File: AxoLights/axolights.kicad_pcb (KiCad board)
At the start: 2 copper layers, 100 x 50 mm, 54 parts, among them IC1 ATTINY85-S, P1 CONN_01X07, Q1 BSS138, Q2 BSS138, Q3 BSS138, Q4 BSS138, Q5 BSS138, Q6 BSS138, Q7 BSS138, Q8 BSS138

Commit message: started routing
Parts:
- removed IC1: ATTINY85-S, Housings_SOIC:SOIJ-8_5.3x5.3mm_Pitch1.27mm
- added P2: CONN_01X07, Connectors_JST:JST_EH_S07B-EH_07x2.50mm_Angled, B.Cu at (202.5, 71.5)
- P1: footprint Pin_Headers:Pin_Header_Straight_1x07_Pitch2.54mm -> Connectors_JST:JST_EH_S07B-EH_07x2.50mm_Angled; moved to B.Cu
- moved P1 89.0 mm to (116.5, 56.5), turned to 270 degrees
- moved Q7 18.0 mm to (202.2, 49.8)
- moved R13 18.0 mm to (205.8, 49.8)
- moved Q8 18.0 mm to (202.0, 78.2)
- moved R15 18.0 mm to (205.0, 78.2)
- moved Q6 14.3 mm to (190.8, 84.5)
- moved R10 14.3 mm to (190.8, 87.5)
- moved Q5 11.9 mm to (178.2, 84.5)
- moved R5 11.9 mm to (178.2, 87.5)
- moved D16 10.2 mm to (190.8, 51.5)
- moved D17 10.2 mm to (190.8, 64.0)
- moved D18 10.2 mm to (190.8, 76.5)
- moved R12 10.2 mm to (190.8, 43.5)
- moved R14 9.92 mm to (116.5, 50.0)
- moved R16 9.92 mm to (116.5, 78.0)
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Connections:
- Q1 pad 1: /AxoLights LEDs/WW -> WW
- Q2 pad 1: /AxoLights LEDs/WW -> WW
- Q3 pad 1: /AxoLights LEDs/NW -> NW
- Q4 pad 1: /AxoLights LEDs/NW -> NW
- Q5 pad 1: /AxoLights LEDs/NW -> NW
- Q6 pad 1: /AxoLights LEDs/KW -> KW
- Q7 pad 1: /AxoLights LEDs/Rt -> Rt
- Q8 pad 1: /AxoLights LEDs/Bl -> Bl
- R1 pad 2: /AxoLights LEDs/WW -> WW
- R10 pad 2: /AxoLights LEDs/KW -> KW
- R13 pad 2: /AxoLights LEDs/Rt -> Rt
- R15 pad 2: /AxoLights LEDs/Bl -> Bl
- R2 pad 2: /AxoLights LEDs/WW -> WW
- R5 pad 2: /AxoLights LEDs/NW -> NW
- R6 pad 2: /AxoLights LEDs/NW -> NW
- R9 pad 2: /AxoLights LEDs/NW -> NW
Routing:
- net GND: track 0.00 -> 151.4 mm, vias 0 -> 7
- net +12V: track 0.00 -> 151.1 mm, vias 0 -> 1
- net Bl: track 0.00 -> 25.4 mm
- net Net-(D23-Pad2): track 0.00 -> 22.5 mm, vias 0 -> 2
- net Net-(D22-Pad2): track 0.00 -> 22.5 mm, vias 0 -> 2
- net Net-(D20-Pad1): track 0.00 -> 22.5 mm, vias 0 -> 2
- net Net-(D19-Pad1): track 0.00 -> 22.5 mm, vias 0 -> 2
- net Net-(D24-Pad2): track 0.00 -> 21.6 mm, vias 0 -> 2
- net Net-(D19-Pad2): track 0.00 -> 18.8 mm, vias 0 -> 2
- net Net-(D21-Pad1): track 0.00 -> 18.6 mm, vias 0 -> 2
- net Net-(D22-Pad1): track 0.00 -> 18.3 mm, vias 0 -> 2
- net Rt: track 0.00 -> 14.5 mm, vias 0 -> 1
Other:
- outline, holes or cut-outs redrawn
- net class Default: trace_width 0.25 -> 0.4
- net class Power: trace_width 1 -> 0.75

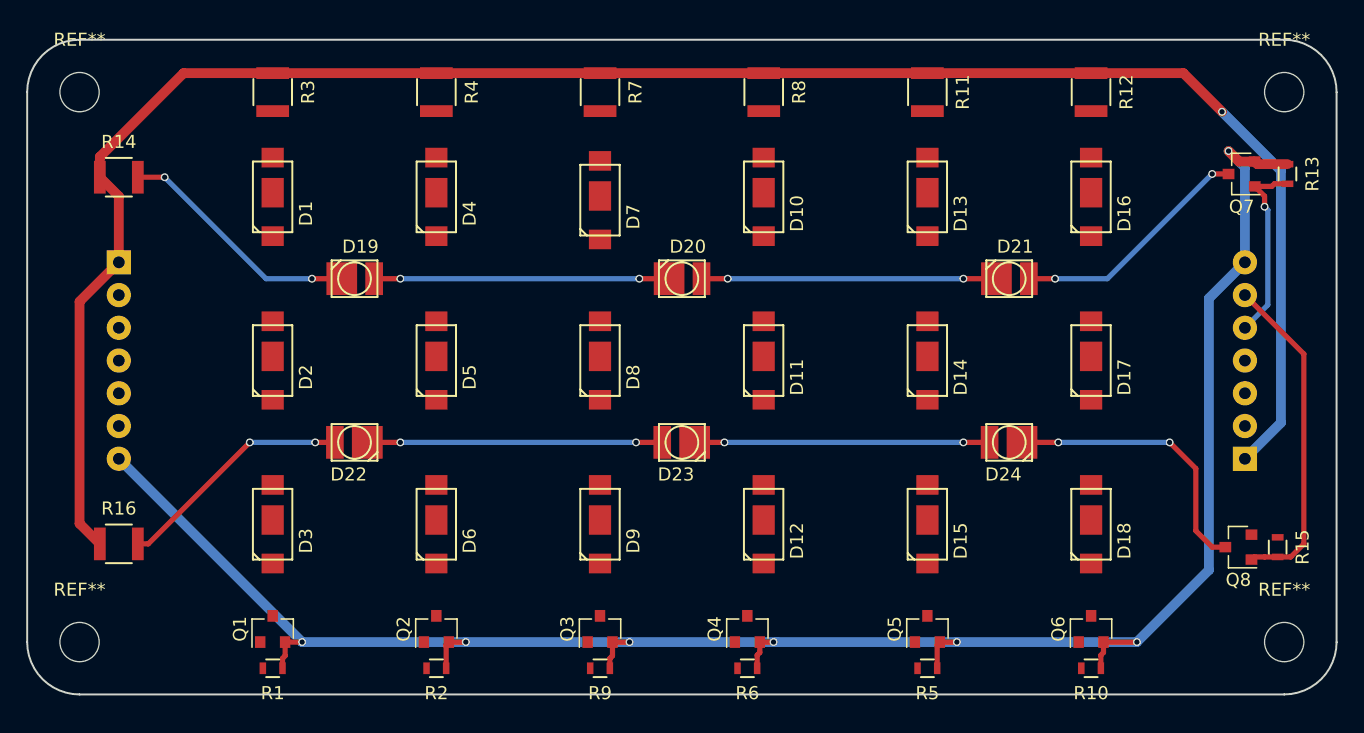
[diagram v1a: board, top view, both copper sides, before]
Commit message: Heatsinks started
started to layout heatsinking planes for LEDs
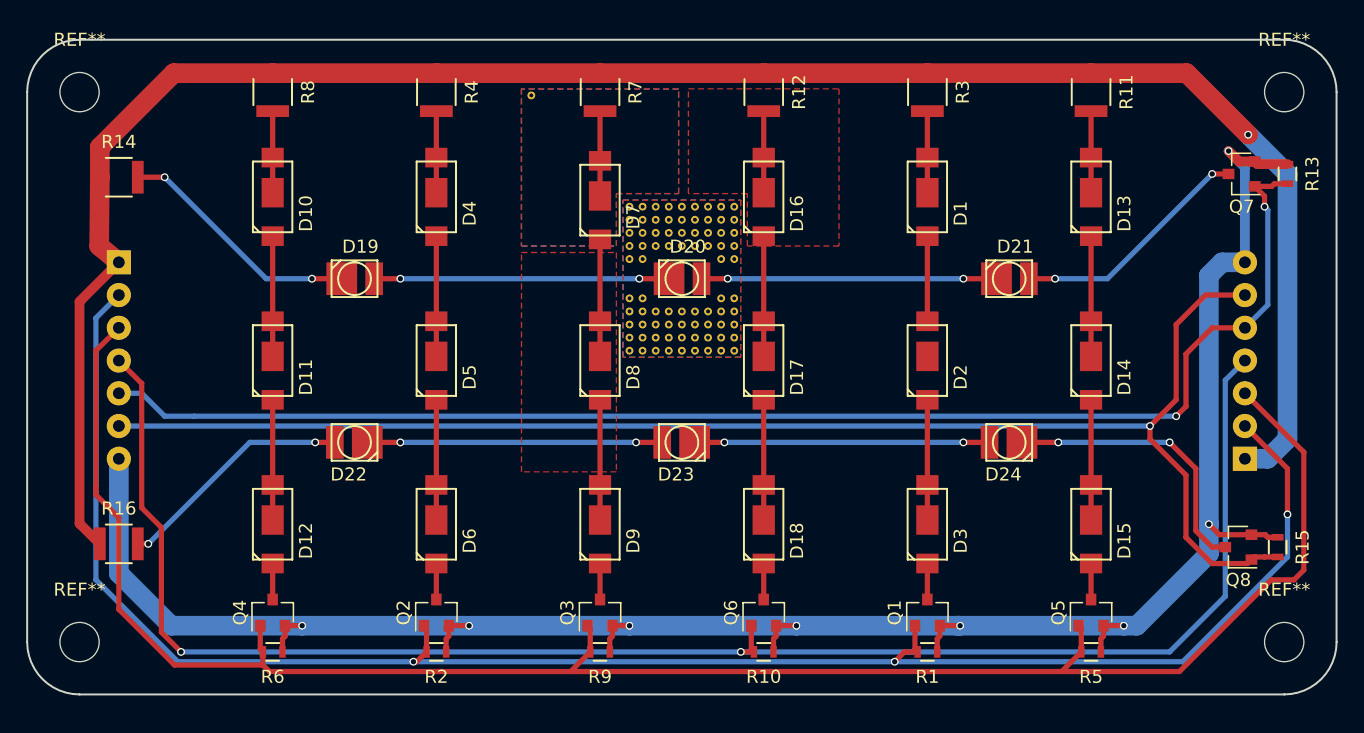
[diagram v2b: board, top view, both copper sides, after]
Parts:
- added REF**: ThermalVia, myfootprint:ThermalVia-0.6, F.Cu at (148.0, 43.8)
- added REF**: ThermalVia, myfootprint:ThermalVia-0.6, F.Cu at (157.5, 63.2)
- added REF**: ThermalVia, myfootprint:ThermalVia-0.6, F.Cu at (156.5, 63.2)
- added REF**: ThermalVia, myfootprint:ThermalVia-0.6, F.Cu at (155.5, 63.2)
- added REF**: ThermalVia, myfootprint:ThermalVia-0.6, F.Cu at (163.5, 62.2)
- added REF**: ThermalVia, myfootprint:ThermalVia-0.6, F.Cu at (162.5, 62.2)
- added REF**: ThermalVia, myfootprint:ThermalVia-0.6, F.Cu at (161.5, 62.2)
- added REF**: ThermalVia, myfootprint:ThermalVia-0.6, F.Cu at (160.5, 62.2)
- added REF**: ThermalVia, myfootprint:ThermalVia-0.6, F.Cu at (159.5, 62.2)
- added REF**: ThermalVia, myfootprint:ThermalVia-0.6, F.Cu at (158.5, 62.2)
- added REF**: ThermalVia, myfootprint:ThermalVia-0.6, F.Cu at (157.5, 62.2)
- added REF**: ThermalVia, myfootprint:ThermalVia-0.6, F.Cu at (158.5, 57.2)
- added REF**: ThermalVia, myfootprint:ThermalVia-0.6, F.Cu at (156.5, 62.2)
- added REF**: ThermalVia, myfootprint:ThermalVia-0.6, F.Cu at (155.5, 62.2)
- added REF**: ThermalVia, myfootprint:ThermalVia-0.6, F.Cu at (163.5, 61.2)
- added REF**: ThermalVia, myfootprint:ThermalVia-0.6, F.Cu at (162.5, 61.2)
- added REF**: ThermalVia, myfootprint:ThermalVia-0.6, F.Cu at (161.5, 61.2)
- added REF**: ThermalVia, myfootprint:ThermalVia-0.6, F.Cu at (160.5, 61.2)
- added REF**: ThermalVia, myfootprint:ThermalVia-0.6, F.Cu at (159.5, 61.2)
- added REF**: ThermalVia, myfootprint:ThermalVia-0.6, F.Cu at (158.5, 61.2)
- added REF**: ThermalVia, myfootprint:ThermalVia-0.6, F.Cu at (157.5, 61.2)
- added REF**: ThermalVia, myfootprint:ThermalVia-0.6, F.Cu at (156.5, 61.2)
- added REF**: ThermalVia, myfootprint:ThermalVia-0.6, F.Cu at (158.5, 58.2)
- added REF**: ThermalVia, myfootprint:ThermalVia-0.6, F.Cu at (155.5, 61.2)
- added REF**: ThermalVia, myfootprint:ThermalVia-0.6, F.Cu at (163.5, 60.2)
- added REF**: ThermalVia, myfootprint:ThermalVia-0.6, F.Cu at (162.5, 60.2)
- added REF**: ThermalVia, myfootprint:ThermalVia-0.6, F.Cu at (161.5, 60.2)
- added REF**: ThermalVia, myfootprint:ThermalVia-0.6, F.Cu at (160.5, 60.2)
- added REF**: ThermalVia, myfootprint:ThermalVia-0.6, F.Cu at (159.5, 60.2)
- added REF**: ThermalVia, myfootprint:ThermalVia-0.6, F.Cu at (158.5, 60.2)
- added REF**: ThermalVia, myfootprint:ThermalVia-0.6, F.Cu at (157.5, 60.2)
- added REF**: ThermalVia, myfootprint:ThermalVia-0.6, F.Cu at (156.5, 60.2)
- added REF**: ThermalVia, myfootprint:ThermalVia-0.6, F.Cu at (155.5, 60.2)
- added REF**: ThermalVia, myfootprint:ThermalVia-0.6, F.Cu at (163.5, 63.2)
- added REF**: ThermalVia, myfootprint:ThermalVia-0.6, F.Cu at (163.5, 59.2)
- added REF**: ThermalVia, myfootprint:ThermalVia-0.6, F.Cu at (162.5, 59.2)
- added REF**: ThermalVia, myfootprint:ThermalVia-0.6, F.Cu at (156.5, 59.2)
- added REF**: ThermalVia, myfootprint:ThermalVia-0.6, F.Cu at (155.5, 59.2)
- added REF**: ThermalVia, myfootprint:ThermalVia-0.6, F.Cu at (163.5, 56.2)
- added REF**: ThermalVia, myfootprint:ThermalVia-0.6, F.Cu at (162.5, 56.2)
- added REF**: ThermalVia, myfootprint:ThermalVia-0.6, F.Cu at (157.5, 56.2)
- added REF**: ThermalVia, myfootprint:ThermalVia-0.6, F.Cu at (156.5, 56.2)
- added REF**: ThermalVia, myfootprint:ThermalVia-0.6, F.Cu at (155.5, 56.2)
- added REF**: ThermalVia, myfootprint:ThermalVia-0.6, F.Cu at (163.5, 55.2)
- added REF**: ThermalVia, myfootprint:ThermalVia-0.6, F.Cu at (162.5, 63.2)
- added REF**: ThermalVia, myfootprint:ThermalVia-0.6, F.Cu at (162.5, 55.2)
- added REF**: ThermalVia, myfootprint:ThermalVia-0.6, F.Cu at (161.5, 55.2)
- added REF**: ThermalVia, myfootprint:ThermalVia-0.6, F.Cu at (160.5, 55.2)
- added REF**: ThermalVia, myfootprint:ThermalVia-0.6, F.Cu at (159.5, 55.2)
- added REF**: ThermalVia, myfootprint:ThermalVia-0.6, F.Cu at (158.5, 55.2)
- added REF**: ThermalVia, myfootprint:ThermalVia-0.6, F.Cu at (157.5, 55.2)
- added REF**: ThermalVia, myfootprint:ThermalVia-0.6, F.Cu at (156.5, 55.2)
- added REF**: ThermalVia, myfootprint:ThermalVia-0.6, F.Cu at (155.5, 55.2)
- added REF**: ThermalVia, myfootprint:ThermalVia-0.6, F.Cu at (163.5, 54.2)
- added REF**: ThermalVia, myfootprint:ThermalVia-0.6, F.Cu at (162.5, 54.2)
- added REF**: ThermalVia, myfootprint:ThermalVia-0.6, F.Cu at (161.5, 63.2)
- added REF**: ThermalVia, myfootprint:ThermalVia-0.6, F.Cu at (161.5, 54.2)
- added REF**: ThermalVia, myfootprint:ThermalVia-0.6, F.Cu at (160.5, 54.2)
- added REF**: ThermalVia, myfootprint:ThermalVia-0.6, F.Cu at (159.5, 54.2)
- added REF**: ThermalVia, myfootprint:ThermalVia-0.6, F.Cu at (158.5, 54.2)
- added REF**: ThermalVia, myfootprint:ThermalVia-0.6, F.Cu at (157.5, 54.2)
- added REF**: ThermalVia, myfootprint:ThermalVia-0.6, F.Cu at (156.5, 54.2)
- added REF**: ThermalVia, myfootprint:ThermalVia-0.6, F.Cu at (155.5, 54.2)
- added REF**: ThermalVia, myfootprint:ThermalVia-0.6, F.Cu at (163.5, 53.2)
- added REF**: ThermalVia, myfootprint:ThermalVia-0.6, F.Cu at (162.5, 53.2)
- added REF**: ThermalVia, myfootprint:ThermalVia-0.6, F.Cu at (161.5, 53.2)
- added REF**: ThermalVia, myfootprint:ThermalVia-0.6, F.Cu at (160.5, 63.2)
- added REF**: ThermalVia, myfootprint:ThermalVia-0.6, F.Cu at (160.5, 53.2)
- added REF**: ThermalVia, myfootprint:ThermalVia-0.6, F.Cu at (159.5, 53.2)
- added REF**: ThermalVia, myfootprint:ThermalVia-0.6, F.Cu at (158.5, 53.2)
- added REF**: ThermalVia, myfootprint:ThermalVia-0.6, F.Cu at (157.5, 53.2)
- added REF**: ThermalVia, myfootprint:ThermalVia-0.6, F.Cu at (156.5, 53.2)
- added REF**: ThermalVia, myfootprint:ThermalVia-0.6, F.Cu at (155.5, 53.2)
- added REF**: ThermalVia, myfootprint:ThermalVia-0.6, F.Cu at (163.5, 52.2)
- added REF**: ThermalVia, myfootprint:ThermalVia-0.6, F.Cu at (162.5, 52.2)
- added REF**: ThermalVia, myfootprint:ThermalVia-0.6, F.Cu at (161.5, 52.2)
- added REF**: ThermalVia, myfootprint:ThermalVia-0.6, F.Cu at (160.5, 52.2)
- added REF**: ThermalVia, myfootprint:ThermalVia-0.6, F.Cu at (159.5, 63.2)
- added REF**: ThermalVia, myfootprint:ThermalVia-0.6, F.Cu at (159.5, 52.2)
- added REF**: ThermalVia, myfootprint:ThermalVia-0.6, F.Cu at (158.5, 52.2)
- added REF**: ThermalVia, myfootprint:ThermalVia-0.6, F.Cu at (157.5, 52.2)
- added REF**: ThermalVia, myfootprint:ThermalVia-0.6, F.Cu at (156.5, 52.2)
- added REF**: ThermalVia, myfootprint:ThermalVia-0.6, F.Cu at (155.5, 52.2)
- added REF**: ThermalVia, myfootprint:ThermalVia-0.6, F.Cu at (158.5, 63.2)
- moved Q1 50.0 mm to (178.2, 83.2)
- moved R1 50.0 mm to (178.2, 86.2)
- moved D1 50.0 mm to (178.2, 51.5)
- moved D2 50.0 mm to (178.2, 64.0)
- moved D3 50.0 mm to (178.2, 76.5)
- moved R3 50.0 mm to (178.2, 43.5)
- moved D10 37.5 mm to (128.2, 51.5)
- moved D11 37.5 mm to (128.2, 64.0)
- moved D12 37.5 mm to (128.2, 76.5)
- moved R8 37.5 mm to (128.2, 43.5)
- moved Q4 36.3 mm to (128.2, 83.2)
- moved R6 36.3 mm to (128.2, 86.2)
- moved Q6 25.0 mm to (165.8, 83.2)
- moved R10 25.0 mm to (165.8, 86.2)
- moved D16 25.0 mm to (165.8, 51.5)
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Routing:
- net NW: track 0.00 -> 145.8 mm
- net WW: track 0.00 -> 138.3 mm, vias 0 -> 3
- net KW: track 0.00 -> 127.4 mm, vias 0 -> 2
- net Rt: track 14.5 -> 106.4 mm, vias 1 -> 2
- net Bl: track 25.4 -> 111.2 mm, vias 0 -> 1
- net GND: track 151.4 -> 162.0 mm, vias 7 -> 8
- net Net-(D8-Pad2): track 0.00 -> 9.18 mm
- net Net-(D5-Pad2): track 0.00 -> 9.18 mm
- net Net-(D2-Pad2): track 0.00 -> 9.18 mm
- net Net-(D17-Pad2): track 0.00 -> 9.18 mm
- net Net-(D14-Pad2): track 0.00 -> 9.18 mm
- net Net-(D11-Pad2): track 0.00 -> 9.18 mm
- net Net-(D4-Pad2): track 0.00 -> 9.18 mm
- net Net-(D16-Pad2): track 0.00 -> 9.18 mm
- net Net-(D13-Pad2): track 0.00 -> 9.18 mm
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- added copper zone on F.Cu, net Net-(D16-Pad1)
- added copper zone on B.Cu, net Net-(D19-Pad1)
- added copper zone on F.Cu, net Net-(D19-Pad1)
- added copper zone on B.Cu, net Net-(D7-Pad1)
- added copper zone on F.Cu, net Net-(D7-Pad1)
- added copper zone on F.Cu, net Net-(D7-Pad2)
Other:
- net class Power: trace_width 0.75 -> 1.5; via_dia 0.6 -> 1.5; via_drill 0.4 -> 0.6
- board text added: "106,625mm²"

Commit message: latest changes for production
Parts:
- added REF**: ThermalVia, myfootprint:ThermalVia-0.6, F.Cu at (151.8, 71.2)
- added REF**: ThermalVia, myfootprint:ThermalVia-0.6, F.Cu at (147.8, 70.2)
- added REF**: ThermalVia, myfootprint:ThermalVia-0.6, F.Cu at (125.8, 69.2)
- added REF**: ThermalVia, myfootprint:ThermalVia-0.6, F.Cu at (195.2, 77.5)
- added REF**: ThermalVia, myfootprint:ThermalVia-0.6, F.Cu at (194.2, 77.5)
- added REF**: ThermalVia, myfootprint:ThermalVia-0.6, F.Cu at (193.2, 77.5)
- added REF**: ThermalVia, myfootprint:ThermalVia-0.6, F.Cu at (189.2, 78.0)
- added REF**: ThermalVia, myfootprint:ThermalVia-0.6, F.Cu at (188.2, 77.5)
- added REF**: ThermalVia, myfootprint:ThermalVia-0.6, F.Cu at (187.2, 77.5)
- added REF**: ThermalVia, myfootprint:ThermalVia-0.6, F.Cu at (186.2, 77.5)
- added REF**: ThermalVia, myfootprint:ThermalVia-0.6, F.Cu at (185.2, 77.5)
- added REF**: ThermalVia, myfootprint:ThermalVia-0.6, F.Cu at (196.2, 76.5)
- added REF**: ThermalVia, myfootprint:ThermalVia-0.6, F.Cu at (195.2, 76.5)
- added REF**: ThermalVia, myfootprint:ThermalVia-0.6, F.Cu at (124.8, 69.2)
- added REF**: ThermalVia, myfootprint:ThermalVia-0.6, F.Cu at (194.2, 76.5)
- added REF**: ThermalVia, myfootprint:ThermalVia-0.6, F.Cu at (193.2, 76.5)
- added REF**: ThermalVia, myfootprint:ThermalVia-0.6, F.Cu at (196.2, 75.5)
- added REF**: ThermalVia, myfootprint:ThermalVia-0.6, F.Cu at (195.2, 75.5)
- added REF**: ThermalVia, myfootprint:ThermalVia-0.6, F.Cu at (194.2, 75.5)
- added REF**: ThermalVia, myfootprint:ThermalVia-0.6, F.Cu at (193.2, 75.5)
- added REF**: ThermalVia, myfootprint:ThermalVia-0.6, F.Cu at (192.2, 78.0)
- added REF**: ThermalVia, myfootprint:ThermalVia-0.6, F.Cu at (196.2, 74.5)
- added REF**: ThermalVia, myfootprint:ThermalVia-0.6, F.Cu at (195.2, 74.5)
- added REF**: ThermalVia, myfootprint:ThermalVia-0.6, F.Cu at (194.2, 74.5)
- added REF**: ThermalVia, myfootprint:ThermalVia-0.6, F.Cu at (123.8, 69.2)
- added REF**: ThermalVia, myfootprint:ThermalVia-0.6, F.Cu at (193.2, 74.5)
- added REF**: ThermalVia, myfootprint:ThermalVia-0.6, F.Cu at (192.2, 74.5)
- added REF**: ThermalVia, myfootprint:ThermalVia-0.6, F.Cu at (196.2, 73.5)
- added REF**: ThermalVia, myfootprint:ThermalVia-0.6, F.Cu at (195.2, 73.5)
- added REF**: ThermalVia, myfootprint:ThermalVia-0.6, F.Cu at (194.2, 73.5)
- added REF**: ThermalVia, myfootprint:ThermalVia-0.6, F.Cu at (193.2, 73.5)
- added REF**: ThermalVia, myfootprint:ThermalVia-0.6, F.Cu at (192.2, 73.5)
- added REF**: ThermalVia, myfootprint:ThermalVia-0.6, F.Cu at (183.7, 84.5)
- added REF**: ThermalVia, myfootprint:ThermalVia-0.6, F.Cu at (182.7, 84.5)
- added REF**: ThermalVia, myfootprint:ThermalVia-0.6, F.Cu at (181.7, 84.5)
- added REF**: ThermalVia, myfootprint:ThermalVia-0.6, F.Cu at (122.8, 69.2)
- added REF**: ThermalVia, myfootprint:ThermalVia-0.6, F.Cu at (180.7, 84.5)
- added REF**: ThermalVia, myfootprint:ThermalVia-0.6, F.Cu at (175.7, 84.5)
- added REF**: ThermalVia, myfootprint:ThermalVia-0.6, F.Cu at (174.7, 84.5)
- added REF**: ThermalVia, myfootprint:ThermalVia-0.6, F.Cu at (173.7, 84.5)
- added REF**: ThermalVia, myfootprint:ThermalVia-0.6, F.Cu at (172.7, 84.5)
- added REF**: ThermalVia, myfootprint:ThermalVia-0.6, F.Cu at (183.7, 83.5)
- added REF**: ThermalVia, myfootprint:ThermalVia-0.6, F.Cu at (182.7, 83.5)
- added REF**: ThermalVia, myfootprint:ThermalVia-0.6, F.Cu at (181.7, 83.5)
- added REF**: ThermalVia, myfootprint:ThermalVia-0.6, F.Cu at (180.7, 83.5)
- added REF**: ThermalVia, myfootprint:ThermalVia-0.6, F.Cu at (175.7, 83.5)
- added REF**: ThermalVia, myfootprint:ThermalVia-0.6, F.Cu at (126.8, 68.2)
- added REF**: ThermalVia, myfootprint:ThermalVia-0.6, F.Cu at (174.7, 83.5)
- added REF**: ThermalVia, myfootprint:ThermalVia-0.6, F.Cu at (173.7, 83.5)
- added REF**: ThermalVia, myfootprint:ThermalVia-0.6, F.Cu at (172.7, 83.5)
- added REF**: ThermalVia, myfootprint:ThermalVia-0.6, F.Cu at (183.7, 82.5)
- added REF**: ThermalVia, myfootprint:ThermalVia-0.6, F.Cu at (182.7, 82.5)
- added REF**: ThermalVia, myfootprint:ThermalVia-0.6, F.Cu at (181.7, 82.5)
- added REF**: ThermalVia, myfootprint:ThermalVia-0.6, F.Cu at (180.7, 82.5)
- added REF**: ThermalVia, myfootprint:ThermalVia-0.6, F.Cu at (179.7, 82.5)
- added REF**: ThermalVia, myfootprint:ThermalVia-0.6, F.Cu at (176.7, 82.5)
- added REF**: ThermalVia, myfootprint:ThermalVia-0.6, F.Cu at (175.7, 82.5)
- added REF**: ThermalVia, myfootprint:ThermalVia-0.6, F.Cu at (125.8, 68.2)
- added REF**: ThermalVia, myfootprint:ThermalVia-0.6, F.Cu at (174.7, 82.5)
- added REF**: ThermalVia, myfootprint:ThermalVia-0.6, F.Cu at (173.7, 82.5)
- added REF**: ThermalVia, myfootprint:ThermalVia-0.6, F.Cu at (172.7, 82.5)
- added REF**: ThermalVia, myfootprint:ThermalVia-0.6, F.Cu at (183.7, 81.5)
- added REF**: ThermalVia, myfootprint:ThermalVia-0.6, F.Cu at (182.7, 81.5)
- added REF**: ThermalVia, myfootprint:ThermalVia-0.6, F.Cu at (181.7, 81.5)
- added REF**: ThermalVia, myfootprint:ThermalVia-0.6, F.Cu at (180.7, 81.5)
- added REF**: ThermalVia, myfootprint:ThermalVia-0.6, F.Cu at (179.7, 81.5)
- added REF**: ThermalVia, myfootprint:ThermalVia-0.6, F.Cu at (176.7, 81.5)
- added REF**: ThermalVia, myfootprint:ThermalVia-0.6, F.Cu at (175.7, 81.5)
- added REF**: ThermalVia, myfootprint:ThermalVia-0.6, F.Cu at (124.8, 68.2)
- added REF**: ThermalVia, myfootprint:ThermalVia-0.6, F.Cu at (174.7, 81.5)
- added REF**: ThermalVia, myfootprint:ThermalVia-0.6, F.Cu at (173.7, 81.5)
- added REF**: ThermalVia, myfootprint:ThermalVia-0.6, F.Cu at (172.7, 81.5)
- added REF**: ThermalVia, myfootprint:ThermalVia-0.6, F.Cu at (183.7, 80.5)
- added REF**: ThermalVia, myfootprint:ThermalVia-0.6, F.Cu at (182.7, 80.5)
- added REF**: ThermalVia, myfootprint:ThermalVia-0.6, F.Cu at (181.7, 80.5)
- added REF**: ThermalVia, myfootprint:ThermalVia-0.6, F.Cu at (180.7, 80.5)
- added REF**: ThermalVia, myfootprint:ThermalVia-0.6, F.Cu at (175.7, 80.5)
- added REF**: ThermalVia, myfootprint:ThermalVia-0.6, F.Cu at (174.7, 80.5)
- added REF**: ThermalVia, myfootprint:ThermalVia-0.6, F.Cu at (173.7, 80.5)
- added REF**: ThermalVia, myfootprint:ThermalVia-0.6, F.Cu at (123.8, 68.2)
- added REF**: ThermalVia, myfootprint:ThermalVia-0.6, F.Cu at (172.7, 80.5)
- added REF**: ThermalVia, myfootprint:ThermalVia-0.6, F.Cu at (183.7, 79.5)
- added REF**: ThermalVia, myfootprint:ThermalVia-0.6, F.Cu at (182.7, 79.5)
- added REF**: ThermalVia, myfootprint:ThermalVia-0.6, F.Cu at (181.7, 79.5)
- added REF**: ThermalVia, myfootprint:ThermalVia-0.6, F.Cu at (180.7, 79.5)
- added REF**: ThermalVia, myfootprint:ThermalVia-0.6, F.Cu at (175.7, 79.5)
- added REF**: ThermalVia, myfootprint:ThermalVia-0.6, F.Cu at (174.7, 79.5)
- added REF**: ThermalVia, myfootprint:ThermalVia-0.6, F.Cu at (173.7, 79.5)
- added REF**: ThermalVia, myfootprint:ThermalVia-0.6, F.Cu at (172.7, 79.5)
- added REF**: ThermalVia, myfootprint:ThermalVia-0.6, F.Cu at (183.7, 78.5)
- added REF**: ThermalVia, myfootprint:ThermalVia-0.6, F.Cu at (122.8, 68.2)
- added REF**: ThermalVia, myfootprint:ThermalVia-0.6, F.Cu at (182.7, 78.5)
- added REF**: ThermalVia, myfootprint:ThermalVia-0.6, F.Cu at (181.7, 78.5)
- added REF**: ThermalVia, myfootprint:ThermalVia-0.6, F.Cu at (180.7, 78.5)
- added REF**: ThermalVia, myfootprint:ThermalVia-0.6, F.Cu at (179.7, 77.9)
- added REF**: ThermalVia, myfootprint:ThermalVia-0.6, F.Cu at (176.7, 77.9)
- added REF**: ThermalVia, myfootprint:ThermalVia-0.6, F.Cu at (175.7, 78.5)
- added REF**: ThermalVia, myfootprint:ThermalVia-0.6, F.Cu at (174.7, 78.5)
- added REF**: ThermalVia, myfootprint:ThermalVia-0.6, F.Cu at (173.7, 78.5)
- added REF**: ThermalVia, myfootprint:ThermalVia-0.6, F.Cu at (172.7, 78.5)
- added REF**: ThermalVia, myfootprint:ThermalVia-0.6, F.Cu at (183.7, 77.5)
- added REF**: ThermalVia, myfootprint:ThermalVia-0.6, F.Cu at (126.8, 67.2)
- added REF**: ThermalVia, myfootprint:ThermalVia-0.6, F.Cu at (182.7, 77.5)
- added REF**: ThermalVia, myfootprint:ThermalVia-0.6, F.Cu at (181.7, 77.5)
- added REF**: ThermalVia, myfootprint:ThermalVia-0.6, F.Cu at (180.7, 77.5)
- added REF**: ThermalVia, myfootprint:ThermalVia-0.6, F.Cu at (175.7, 77.5)
- added REF**: ThermalVia, myfootprint:ThermalVia-0.6, F.Cu at (174.7, 77.5)
- added REF**: ThermalVia, myfootprint:ThermalVia-0.6, F.Cu at (173.7, 77.5)
- added REF**: ThermalVia, myfootprint:ThermalVia-0.6, F.Cu at (172.7, 77.5)
- added REF**: ThermalVia, myfootprint:ThermalVia-0.6, F.Cu at (176.7, 76.1)
- added REF**: ThermalVia, myfootprint:ThermalVia-0.6, F.Cu at (175.7, 76.5)
- added REF**: ThermalVia, myfootprint:ThermalVia-0.6, F.Cu at (174.7, 76.5)
- added REF**: ThermalVia, myfootprint:ThermalVia-0.6, F.Cu at (151.8, 69.2)
- added REF**: ThermalVia, myfootprint:ThermalVia-0.6, F.Cu at (125.8, 67.2)
- added REF**: ThermalVia, myfootprint:ThermalVia-0.6, F.Cu at (173.7, 76.5)
- added REF**: ThermalVia, myfootprint:ThermalVia-0.6, F.Cu at (172.7, 76.5)
- added REF**: ThermalVia, myfootprint:ThermalVia-0.6, F.Cu at (175.7, 75.5)
- added REF**: ThermalVia, myfootprint:ThermalVia-0.6, F.Cu at (174.7, 75.5)
- added REF**: ThermalVia, myfootprint:ThermalVia-0.6, F.Cu at (173.7, 75.5)
- added REF**: ThermalVia, myfootprint:ThermalVia-0.6, F.Cu at (172.7, 75.5)
- added REF**: ThermalVia, myfootprint:ThermalVia-0.6, F.Cu at (176.7, 74.5)
- added REF**: ThermalVia, myfootprint:ThermalVia-0.6, F.Cu at (175.7, 74.5)
- added REF**: ThermalVia, myfootprint:ThermalVia-0.6, F.Cu at (174.7, 74.5)
- added REF**: ThermalVia, myfootprint:ThermalVia-0.6, F.Cu at (173.7, 74.5)
- added REF**: ThermalVia, myfootprint:ThermalVia-0.6, F.Cu at (124.8, 67.2)
- added REF**: ThermalVia, myfootprint:ThermalVia-0.6, F.Cu at (172.7, 74.5)
- added REF**: ThermalVia, myfootprint:ThermalVia-0.6, F.Cu at (176.7, 73.5)
- added REF**: ThermalVia, myfootprint:ThermalVia-0.6, F.Cu at (175.7, 73.5)
- added REF**: ThermalVia, myfootprint:ThermalVia-0.6, F.Cu at (174.7, 73.5)
- added REF**: ThermalVia, myfootprint:ThermalVia-0.6, F.Cu at (173.7, 73.5)
- added REF**: ThermalVia, myfootprint:ThermalVia-0.6, F.Cu at (172.7, 73.5)
- added REF**: ThermalVia, myfootprint:ThermalVia-0.6, F.Cu at (171.2, 84.5)
- added REF**: ThermalVia, myfootprint:ThermalVia-0.6, F.Cu at (170.2, 84.5)
- added REF**: ThermalVia, myfootprint:ThermalVia-0.6, F.Cu at (169.2, 84.5)
- added REF**: ThermalVia, myfootprint:ThermalVia-0.6, F.Cu at (168.2, 84.5)
- added REF**: ThermalVia, myfootprint:ThermalVia-0.6, F.Cu at (123.8, 67.2)
- added REF**: ThermalVia, myfootprint:ThermalVia-0.6, F.Cu at (163.2, 84.5)
- added REF**: ThermalVia, myfootprint:ThermalVia-0.6, F.Cu at (162.2, 84.5)
- added REF**: ThermalVia, myfootprint:ThermalVia-0.6, F.Cu at (161.2, 84.5)
- added REF**: ThermalVia, myfootprint:ThermalVia-0.6, F.Cu at (160.2, 84.5)
- added REF**: ThermalVia, myfootprint:ThermalVia-0.6, F.Cu at (171.2, 83.5)
- added REF**: ThermalVia, myfootprint:ThermalVia-0.6, F.Cu at (170.2, 83.5)
- added REF**: ThermalVia, myfootprint:ThermalVia-0.6, F.Cu at (169.2, 83.5)
- added REF**: ThermalVia, myfootprint:ThermalVia-0.6, F.Cu at (168.2, 83.5)
- added REF**: ThermalVia, myfootprint:ThermalVia-0.6, F.Cu at (163.2, 83.5)
- added REF**: ThermalVia, myfootprint:ThermalVia-0.6, F.Cu at (162.2, 83.5)
- added REF**: ThermalVia, myfootprint:ThermalVia-0.6, F.Cu at (122.8, 67.2)
- added REF**: ThermalVia, myfootprint:ThermalVia-0.6, F.Cu at (161.2, 83.5)
- added REF**: ThermalVia, myfootprint:ThermalVia-0.6, F.Cu at (160.2, 83.5)
- added REF**: ThermalVia, myfootprint:ThermalVia-0.6, F.Cu at (171.2, 82.5)
- added REF**: ThermalVia, myfootprint:ThermalVia-0.6, F.Cu at (170.2, 82.5)
- added REF**: ThermalVia, myfootprint:ThermalVia-0.6, F.Cu at (169.2, 82.5)
- added REF**: ThermalVia, myfootprint:ThermalVia-0.6, F.Cu at (168.2, 82.5)
- added REF**: ThermalVia, myfootprint:ThermalVia-0.6, F.Cu at (167.2, 82.5)
- added REF**: ThermalVia, myfootprint:ThermalVia-0.6, F.Cu at (164.2, 82.5)
- added REF**: ThermalVia, myfootprint:ThermalVia-0.6, F.Cu at (163.2, 82.5)
- added REF**: ThermalVia, myfootprint:ThermalVia-0.6, F.Cu at (162.2, 82.5)
- added REF**: ThermalVia, myfootprint:ThermalVia-0.6, F.Cu at (126.8, 66.2)
- added REF**: ThermalVia, myfootprint:ThermalVia-0.6, F.Cu at (161.2, 82.5)
- added REF**: ThermalVia, myfootprint:ThermalVia-0.6, F.Cu at (160.2, 82.5)
- added REF**: ThermalVia, myfootprint:ThermalVia-0.6, F.Cu at (171.2, 81.5)
- added REF**: ThermalVia, myfootprint:ThermalVia-0.6, F.Cu at (170.2, 81.5)
- added REF**: ThermalVia, myfootprint:ThermalVia-0.6, F.Cu at (169.2, 81.5)
- added REF**: ThermalVia, myfootprint:ThermalVia-0.6, F.Cu at (168.2, 81.5)
- added REF**: ThermalVia, myfootprint:ThermalVia-0.6, F.Cu at (167.2, 81.5)
- added REF**: ThermalVia, myfootprint:ThermalVia-0.6, F.Cu at (164.2, 81.5)
- added REF**: ThermalVia, myfootprint:ThermalVia-0.6, F.Cu at (163.2, 81.5)
- added REF**: ThermalVia, myfootprint:ThermalVia-0.6, F.Cu at (162.2, 81.5)
- added REF**: ThermalVia, myfootprint:ThermalVia-0.6, F.Cu at (125.8, 66.2)
- added REF**: ThermalVia, myfootprint:ThermalVia-0.6, F.Cu at (161.2, 81.5)
- added REF**: ThermalVia, myfootprint:ThermalVia-0.6, F.Cu at (160.2, 81.5)
- added REF**: ThermalVia, myfootprint:ThermalVia-0.6, F.Cu at (171.2, 80.5)
- added REF**: ThermalVia, myfootprint:ThermalVia-0.6, F.Cu at (170.2, 80.5)
- added REF**: ThermalVia, myfootprint:ThermalVia-0.6, F.Cu at (169.2, 80.5)
- added REF**: ThermalVia, myfootprint:ThermalVia-0.6, F.Cu at (168.2, 80.5)
- added REF**: ThermalVia, myfootprint:ThermalVia-0.6, F.Cu at (163.2, 80.5)
- added REF**: ThermalVia, myfootprint:ThermalVia-0.6, F.Cu at (162.2, 80.5)
- added REF**: ThermalVia, myfootprint:ThermalVia-0.6, F.Cu at (161.2, 80.5)
- added REF**: ThermalVia, myfootprint:ThermalVia-0.6, F.Cu at (160.2, 80.5)
- added REF**: ThermalVia, myfootprint:ThermalVia-0.6, F.Cu at (124.8, 66.2)
- added REF**: ThermalVia, myfootprint:ThermalVia-0.6, F.Cu at (171.2, 79.5)
- added REF**: ThermalVia, myfootprint:ThermalVia-0.6, F.Cu at (170.2, 79.5)
- added REF**: ThermalVia, myfootprint:ThermalVia-0.6, F.Cu at (169.2, 79.5)
- added REF**: ThermalVia, myfootprint:ThermalVia-0.6, F.Cu at (168.2, 79.5)
- added REF**: ThermalVia, myfootprint:ThermalVia-0.6, F.Cu at (163.2, 79.5)
- added REF**: ThermalVia, myfootprint:ThermalVia-0.6, F.Cu at (162.2, 79.5)
- added REF**: ThermalVia, myfootprint:ThermalVia-0.6, F.Cu at (161.2, 79.5)
- added REF**: ThermalVia, myfootprint:ThermalVia-0.6, F.Cu at (160.2, 79.5)
- added REF**: ThermalVia, myfootprint:ThermalVia-0.6, F.Cu at (171.2, 78.5)
- added REF**: ThermalVia, myfootprint:ThermalVia-0.6, F.Cu at (170.2, 78.5)
- added REF**: ThermalVia, myfootprint:ThermalVia-0.6, F.Cu at (123.8, 66.2)
- added REF**: ThermalVia, myfootprint:ThermalVia-0.6, F.Cu at (169.2, 78.5)
- added REF**: ThermalVia, myfootprint:ThermalVia-0.6, F.Cu at (168.2, 78.5)
- added REF**: ThermalVia, myfootprint:ThermalVia-0.6, F.Cu at (167.1, 77.9)
- added REF**: ThermalVia, myfootprint:ThermalVia-0.6, F.Cu at (164.1, 77.9)
- added REF**: ThermalVia, myfootprint:ThermalVia-0.6, F.Cu at (163.2, 78.5)
- added REF**: ThermalVia, myfootprint:ThermalVia-0.6, F.Cu at (162.2, 78.5)
- added REF**: ThermalVia, myfootprint:ThermalVia-0.6, F.Cu at (161.2, 78.5)
- added REF**: ThermalVia, myfootprint:ThermalVia-0.6, F.Cu at (160.2, 78.5)
- added REF**: ThermalVia, myfootprint:ThermalVia-0.6, F.Cu at (171.2, 77.5)
- added REF**: ThermalVia, myfootprint:ThermalVia-0.6, F.Cu at (170.2, 77.5)
- added REF**: ThermalVia, myfootprint:ThermalVia-0.6, F.Cu at (122.8, 66.2)
- added REF**: ThermalVia, myfootprint:ThermalVia-0.6, F.Cu at (169.2, 77.5)
- added REF**: ThermalVia, myfootprint:ThermalVia-0.6, F.Cu at (168.2, 77.5)
- added REF**: ThermalVia, myfootprint:ThermalVia-0.6, F.Cu at (163.2, 77.5)
- added REF**: ThermalVia, myfootprint:ThermalVia-0.6, F.Cu at (162.2, 77.5)
- added REF**: ThermalVia, myfootprint:ThermalVia-0.6, F.Cu at (161.2, 77.5)
- added REF**: ThermalVia, myfootprint:ThermalVia-0.6, F.Cu at (160.2, 77.5)
- added REF**: ThermalVia, myfootprint:ThermalVia-0.6, F.Cu at (171.2, 76.5)
- added REF**: ThermalVia, myfootprint:ThermalVia-0.6, F.Cu at (170.2, 76.5)
- added REF**: ThermalVia, myfootprint:ThermalVia-0.6, F.Cu at (169.2, 76.5)
- added REF**: ThermalVia, myfootprint:ThermalVia-0.6, F.Cu at (168.2, 76.5)
- added REF**: ThermalVia, myfootprint:ThermalVia-0.6, F.Cu at (126.8, 65.2)
- added REF**: ThermalVia, myfootprint:ThermalVia-0.6, F.Cu at (167.1, 76.1)
- added REF**: ThermalVia, myfootprint:ThermalVia-0.6, F.Cu at (171.2, 75.5)
- added REF**: ThermalVia, myfootprint:ThermalVia-0.6, F.Cu at (170.2, 75.5)
- added REF**: ThermalVia, myfootprint:ThermalVia-0.6, F.Cu at (169.2, 75.5)
- added REF**: ThermalVia, myfootprint:ThermalVia-0.6, F.Cu at (168.2, 75.5)
- added REF**: ThermalVia, myfootprint:ThermalVia-0.6, F.Cu at (171.2, 74.5)
- added REF**: ThermalVia, myfootprint:ThermalVia-0.6, F.Cu at (170.2, 74.5)
- added REF**: ThermalVia, myfootprint:ThermalVia-0.6, F.Cu at (169.2, 74.5)
- added REF**: ThermalVia, myfootprint:ThermalVia-0.6, F.Cu at (168.2, 74.5)
- added REF**: ThermalVia, myfootprint:ThermalVia-0.6, F.Cu at (167.2, 74.5)
- added REF**: ThermalVia, myfootprint:ThermalVia-0.6, F.Cu at (150.8, 69.2)
- added REF**: ThermalVia, myfootprint:ThermalVia-0.6, F.Cu at (125.8, 65.2)
- added REF**: ThermalVia, myfootprint:ThermalVia-0.6, F.Cu at (171.2, 73.5)
- added REF**: ThermalVia, myfootprint:ThermalVia-0.6, F.Cu at (170.2, 73.5)
- added REF**: ThermalVia, myfootprint:ThermalVia-0.6, F.Cu at (169.2, 73.5)
- added REF**: ThermalVia, myfootprint:ThermalVia-0.6, F.Cu at (168.2, 73.5)
- added REF**: ThermalVia, myfootprint:ThermalVia-0.6, F.Cu at (167.2, 73.5)
- added REF**: ThermalVia, myfootprint:ThermalVia-0.6, F.Cu at (158.8, 84.5)
- added REF**: ThermalVia, myfootprint:ThermalVia-0.6, F.Cu at (157.8, 84.5)
- added REF**: ThermalVia, myfootprint:ThermalVia-0.6, F.Cu at (156.8, 84.5)
- added REF**: ThermalVia, myfootprint:ThermalVia-0.6, F.Cu at (155.8, 84.5)
- added REF**: ThermalVia, myfootprint:ThermalVia-0.6, F.Cu at (150.8, 84.5)
- added REF**: ThermalVia, myfootprint:ThermalVia-0.6, F.Cu at (124.8, 65.2)
- added REF**: ThermalVia, myfootprint:ThermalVia-0.6, F.Cu at (149.8, 84.5)
- added REF**: ThermalVia, myfootprint:ThermalVia-0.6, F.Cu at (148.8, 84.5)
- added REF**: ThermalVia, myfootprint:ThermalVia-0.6, F.Cu at (147.8, 84.5)
- added REF**: ThermalVia, myfootprint:ThermalVia-0.6, F.Cu at (158.8, 83.5)
- added REF**: ThermalVia, myfootprint:ThermalVia-0.6, F.Cu at (157.8, 83.5)
- added REF**: ThermalVia, myfootprint:ThermalVia-0.6, F.Cu at (156.8, 83.5)
- added REF**: ThermalVia, myfootprint:ThermalVia-0.6, F.Cu at (155.8, 83.5)
- added REF**: ThermalVia, myfootprint:ThermalVia-0.6, F.Cu at (150.8, 83.5)
- added REF**: ThermalVia, myfootprint:ThermalVia-0.6, F.Cu at (149.8, 83.5)
- added REF**: ThermalVia, myfootprint:ThermalVia-0.6, F.Cu at (148.8, 83.5)
- added REF**: ThermalVia, myfootprint:ThermalVia-0.6, F.Cu at (123.8, 65.2)
- added REF**: ThermalVia, myfootprint:ThermalVia-0.6, F.Cu at (147.8, 83.5)
- added REF**: ThermalVia, myfootprint:ThermalVia-0.6, F.Cu at (158.8, 82.5)
- added REF**: ThermalVia, myfootprint:ThermalVia-0.6, F.Cu at (157.8, 82.5)
- added REF**: ThermalVia, myfootprint:ThermalVia-0.6, F.Cu at (156.8, 82.5)
- added REF**: ThermalVia, myfootprint:ThermalVia-0.6, F.Cu at (155.8, 82.5)
- added REF**: ThermalVia, myfootprint:ThermalVia-0.6, F.Cu at (154.8, 82.5)
- added REF**: ThermalVia, myfootprint:ThermalVia-0.6, F.Cu at (151.8, 82.5)
- added REF**: ThermalVia, myfootprint:ThermalVia-0.6, F.Cu at (150.8, 82.5)
- added REF**: ThermalVia, myfootprint:ThermalVia-0.6, F.Cu at (149.8, 82.5)
- added REF**: ThermalVia, myfootprint:ThermalVia-0.6, F.Cu at (148.8, 82.5)
- added REF**: ThermalVia, myfootprint:ThermalVia-0.6, F.Cu at (122.8, 65.2)
- added REF**: ThermalVia, myfootprint:ThermalVia-0.6, F.Cu at (147.8, 82.5)
- added REF**: ThermalVia, myfootprint:ThermalVia-0.6, F.Cu at (158.8, 81.5)
- added REF**: ThermalVia, myfootprint:ThermalVia-0.6, F.Cu at (157.8, 81.5)
- added REF**: ThermalVia, myfootprint:ThermalVia-0.6, F.Cu at (156.8, 81.5)
- added REF**: ThermalVia, myfootprint:ThermalVia-0.6, F.Cu at (155.8, 81.5)
- added REF**: ThermalVia, myfootprint:ThermalVia-0.6, F.Cu at (154.8, 81.5)
- added REF**: ThermalVia, myfootprint:ThermalVia-0.6, F.Cu at (151.8, 81.5)
- added REF**: ThermalVia, myfootprint:ThermalVia-0.6, F.Cu at (150.8, 81.5)
- added REF**: ThermalVia, myfootprint:ThermalVia-0.6, F.Cu at (149.8, 81.5)
- added REF**: ThermalVia, myfootprint:ThermalVia-0.6, F.Cu at (148.8, 81.5)
- added REF**: ThermalVia, myfootprint:ThermalVia-0.6, F.Cu at (126.8, 64.2)
- added REF**: ThermalVia, myfootprint:ThermalVia-0.6, F.Cu at (147.8, 81.5)
- added REF**: ThermalVia, myfootprint:ThermalVia-0.6, F.Cu at (158.8, 80.5)
- added REF**: ThermalVia, myfootprint:ThermalVia-0.6, F.Cu at (157.8, 80.5)
- added REF**: ThermalVia, myfootprint:ThermalVia-0.6, F.Cu at (156.8, 80.5)
- added REF**: ThermalVia, myfootprint:ThermalVia-0.6, F.Cu at (155.8, 80.5)
- added REF**: ThermalVia, myfootprint:ThermalVia-0.6, F.Cu at (150.8, 80.5)
- added REF**: ThermalVia, myfootprint:ThermalVia-0.6, F.Cu at (149.8, 80.5)
- added REF**: ThermalVia, myfootprint:ThermalVia-0.6, F.Cu at (148.8, 80.5)
- added REF**: ThermalVia, myfootprint:ThermalVia-0.6, F.Cu at (147.8, 80.5)
- added REF**: ThermalVia, myfootprint:ThermalVia-0.6, F.Cu at (158.8, 79.5)
- added REF**: ThermalVia, myfootprint:ThermalVia-0.6, F.Cu at (125.8, 64.2)
- added REF**: ThermalVia, myfootprint:ThermalVia-0.6, F.Cu at (157.8, 79.5)
- added REF**: ThermalVia, myfootprint:ThermalVia-0.6, F.Cu at (156.8, 79.5)
- added REF**: ThermalVia, myfootprint:ThermalVia-0.6, F.Cu at (155.8, 79.5)
- added REF**: ThermalVia, myfootprint:ThermalVia-0.6, F.Cu at (150.8, 79.5)
- added REF**: ThermalVia, myfootprint:ThermalVia-0.6, F.Cu at (149.8, 79.5)
- added REF**: ThermalVia, myfootprint:ThermalVia-0.6, F.Cu at (148.8, 79.5)
- added REF**: ThermalVia, myfootprint:ThermalVia-0.6, F.Cu at (147.8, 79.5)
- added REF**: ThermalVia, myfootprint:ThermalVia-0.6, F.Cu at (158.8, 78.5)
- added REF**: ThermalVia, myfootprint:ThermalVia-0.6, F.Cu at (157.8, 78.5)
- added REF**: ThermalVia, myfootprint:ThermalVia-0.6, F.Cu at (156.8, 78.5)
- added REF**: ThermalVia, myfootprint:ThermalVia-0.6, F.Cu at (124.8, 64.2)
- added REF**: ThermalVia, myfootprint:ThermalVia-0.6, F.Cu at (155.8, 78.5)
- added REF**: ThermalVia, myfootprint:ThermalVia-0.6, F.Cu at (150.8, 78.5)
- added REF**: ThermalVia, myfootprint:ThermalVia-0.6, F.Cu at (149.8, 78.5)
- added REF**: ThermalVia, myfootprint:ThermalVia-0.6, F.Cu at (148.8, 78.5)
- added REF**: ThermalVia, myfootprint:ThermalVia-0.6, F.Cu at (147.8, 78.5)
- added REF**: ThermalVia, myfootprint:ThermalVia-0.6, F.Cu at (158.8, 77.5)
- added REF**: ThermalVia, myfootprint:ThermalVia-0.6, F.Cu at (157.8, 77.5)
- added REF**: ThermalVia, myfootprint:ThermalVia-0.6, F.Cu at (156.8, 77.5)
- added REF**: ThermalVia, myfootprint:ThermalVia-0.6, F.Cu at (155.8, 77.5)
- added REF**: ThermalVia, myfootprint:ThermalVia-0.6, F.Cu at (154.7, 77.9)
- added REF**: ThermalVia, myfootprint:ThermalVia-0.6, F.Cu at (123.8, 64.2)
- added REF**: ThermalVia, myfootprint:ThermalVia-0.6, F.Cu at (151.7, 77.9)
- added REF**: ThermalVia, myfootprint:ThermalVia-0.6, F.Cu at (150.8, 77.5)
- added REF**: ThermalVia, myfootprint:ThermalVia-0.6, F.Cu at (149.8, 77.5)
- added REF**: ThermalVia, myfootprint:ThermalVia-0.6, F.Cu at (148.8, 77.5)
- added REF**: ThermalVia, myfootprint:ThermalVia-0.6, F.Cu at (147.8, 77.5)
- added REF**: ThermalVia, myfootprint:ThermalVia-0.6, F.Cu at (151.7, 76.1)
- added REF**: ThermalVia, myfootprint:ThermalVia-0.6, F.Cu at (150.8, 76.5)
- added REF**: ThermalVia, myfootprint:ThermalVia-0.6, F.Cu at (149.8, 76.5)
- added REF**: ThermalVia, myfootprint:ThermalVia-0.6, F.Cu at (148.8, 76.5)
- added REF**: ThermalVia, myfootprint:ThermalVia-0.6, F.Cu at (147.8, 76.5)
- added REF**: ThermalVia, myfootprint:ThermalVia-0.6, F.Cu at (122.8, 64.2)
- added REF**: ThermalVia, myfootprint:ThermalVia-0.6, F.Cu at (150.8, 75.5)
- added REF**: ThermalVia, myfootprint:ThermalVia-0.6, F.Cu at (149.8, 75.5)
- added REF**: ThermalVia, myfootprint:ThermalVia-0.6, F.Cu at (148.8, 75.5)
- added REF**: ThermalVia, myfootprint:ThermalVia-0.6, F.Cu at (147.8, 75.5)
- added REF**: ThermalVia, myfootprint:ThermalVia-0.6, F.Cu at (151.8, 74.5)
- added REF**: ThermalVia, myfootprint:ThermalVia-0.6, F.Cu at (150.8, 74.5)
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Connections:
- P1 pad 7: GND -> OneWire
- P2 pad 7: GND -> OneWire
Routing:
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- added copper zone on B.Cu, net Net-(D1-Pad1)
- added copper zone on F.Cu, net Net-(D1-Pad1)
- added copper zone on B.Cu, net Net-(D1-Pad2)
- added copper zone on F.Cu, net Net-(D1-Pad2)
- added copper zone on B.Cu, net Net-(D10-Pad1)
- added copper zone on F.Cu, net Net-(D10-Pad1)
- added copper zone on B.Cu, net Net-(D10-Pad2)
- added copper zone on F.Cu, net Net-(D10-Pad2)
- added copper zone on B.Cu, net Net-(D11-Pad2)
- added copper zone on F.Cu, net Net-(D11-Pad2)
- added copper zone on B.Cu, net Net-(D13-Pad1)
- added copper zone on F.Cu, net Net-(D13-Pad1)
- added copper zone on B.Cu, net Net-(D13-Pad2)
- added copper zone on F.Cu, net Net-(D13-Pad2)
- added copper zone on B.Cu, net Net-(D14-Pad2)
- added copper zone on F.Cu, net Net-(D14-Pad2)
- added copper zone on B.Cu, net Net-(D16-Pad1)
- added copper zone on B.Cu, net Net-(D16-Pad2)
- added copper zone on F.Cu, net Net-(D16-Pad2)
- added copper zone on B.Cu, net Net-(D17-Pad2)
- added copper zone on F.Cu, net Net-(D17-Pad2)
- added copper zone on B.Cu, net Net-(D19-Pad2)
- added copper zone on F.Cu, net Net-(D19-Pad2)
- added copper zone on B.Cu, net Net-(D2-Pad2)
- added copper zone on F.Cu, net Net-(D2-Pad2)
- added copper zone on B.Cu, net Net-(D20-Pad1)
- added copper zone on F.Cu, net Net-(D20-Pad1)
- added copper zone on B.Cu, net Net-(D22-Pad2)
- added copper zone on F.Cu, net Net-(D22-Pad2)
- added copper zone on B.Cu, net Net-(D23-Pad2)
- added copper zone on F.Cu, net Net-(D23-Pad2)
- added copper zone on B.Cu, net Net-(D24-Pad2)
- added copper zone on F.Cu, net Net-(D24-Pad2)
- added copper zone on B.Cu, net Net-(D4-Pad1)
- added copper zone on F.Cu, net Net-(D4-Pad1)
- added copper zone on B.Cu, net Net-(D4-Pad2)
- added copper zone on F.Cu, net Net-(D4-Pad2)
- added copper zone on B.Cu, net Net-(D5-Pad2)
- added copper zone on F.Cu, net Net-(D5-Pad2)
- added copper zone on B.Cu, net Net-(D7-Pad2)
- added copper zone on B.Cu, net Net-(D8-Pad2)
- added copper zone on F.Cu, net Net-(D8-Pad2)
